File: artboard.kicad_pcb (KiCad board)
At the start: 2 copper layers, 94.7 x 47.4 mm, 25 parts, among them J2 OLED, SW1 SW_PUSH, SW2 SW_PUSH, SW22 SW_SPDT, SW23 SW_SPDT, SW3 SW_PUSH, SW4 SW_PUSH, SW5 SW_PUSH, SW6 SW_PUSH, SW7 SW_PUSH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

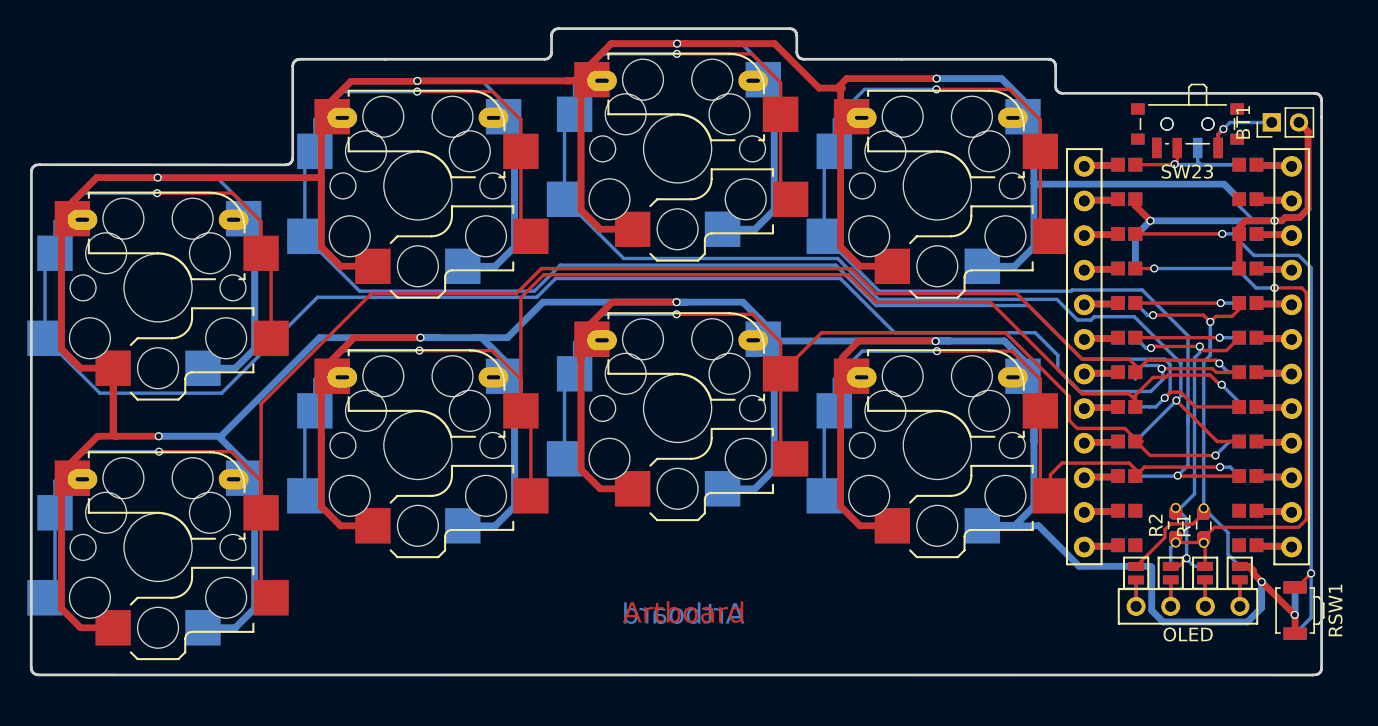
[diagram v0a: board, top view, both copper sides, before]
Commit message: add mounting holes
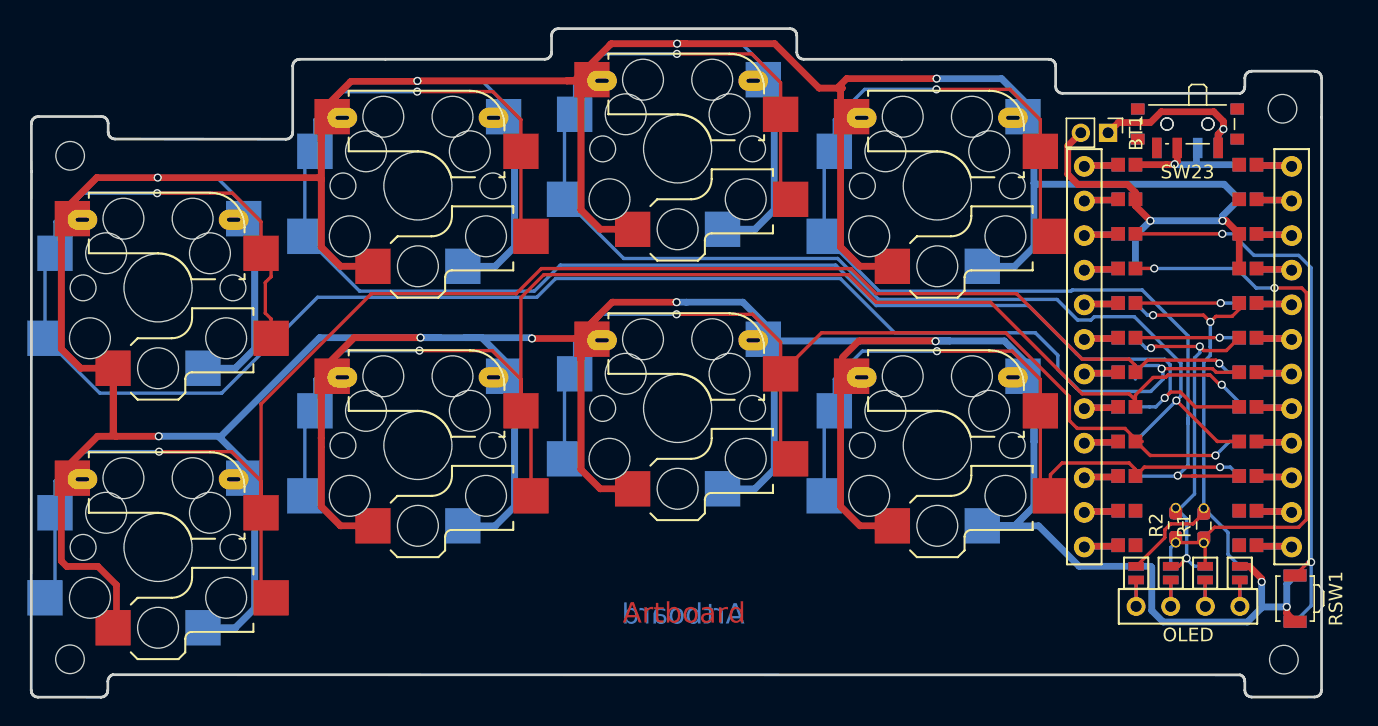
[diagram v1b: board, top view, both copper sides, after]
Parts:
- added Ref**: Val**, MountingHole:MountingHole_2.1mm, F.Cu at (123.8, 76.2)
- added Ref**: Val**, MountingHole:MountingHole_2.1mm, F.Cu at (123.7, 35.8)
- added Ref**: Val**, MountingHole:MountingHole_2.1mm, F.Cu at (34.7, 76.2)
- added Ref**: Val**, MountingHole:MountingHole_2.1mm, F.Cu at (34.7, 39.3)
- moved BT1 12.0 mm to (110.9, 37.6), turned to 270 degrees
- moved RSW1 0.88 mm to (124.7, 71.8)
- moved RSW2 0.88 mm to (124.7, 71.8)
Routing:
- net GND: track 939.4 -> 887.3 mm, vias 12 -> 13
- net Net-(BT1-Pad1): track 6.84 -> 13.1 mm
- net raw: track 15.1 -> 13.0 mm
- net reset: track 43.2 -> 42.3 mm
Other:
- board size 94.7 x 47.4 mm -> 94.7 x 49.1 mm

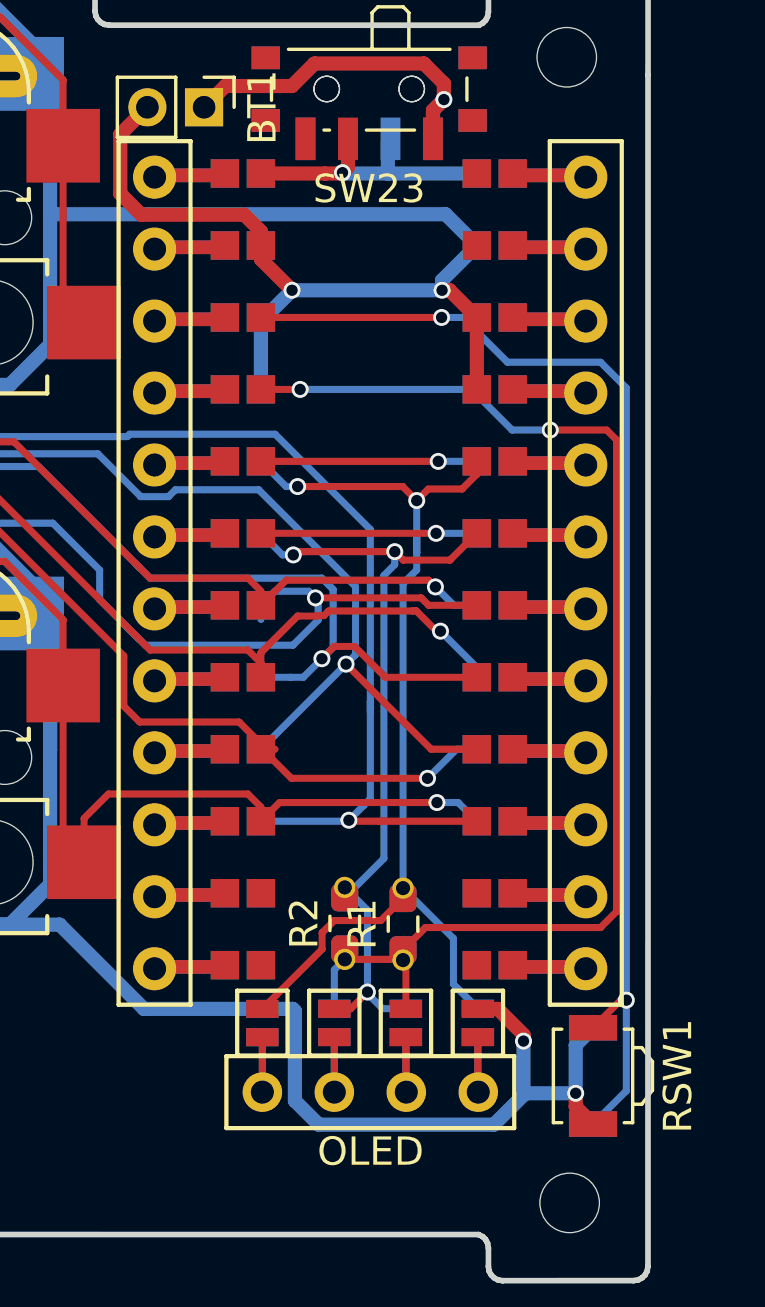
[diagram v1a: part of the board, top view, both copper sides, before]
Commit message: route last dangling pads
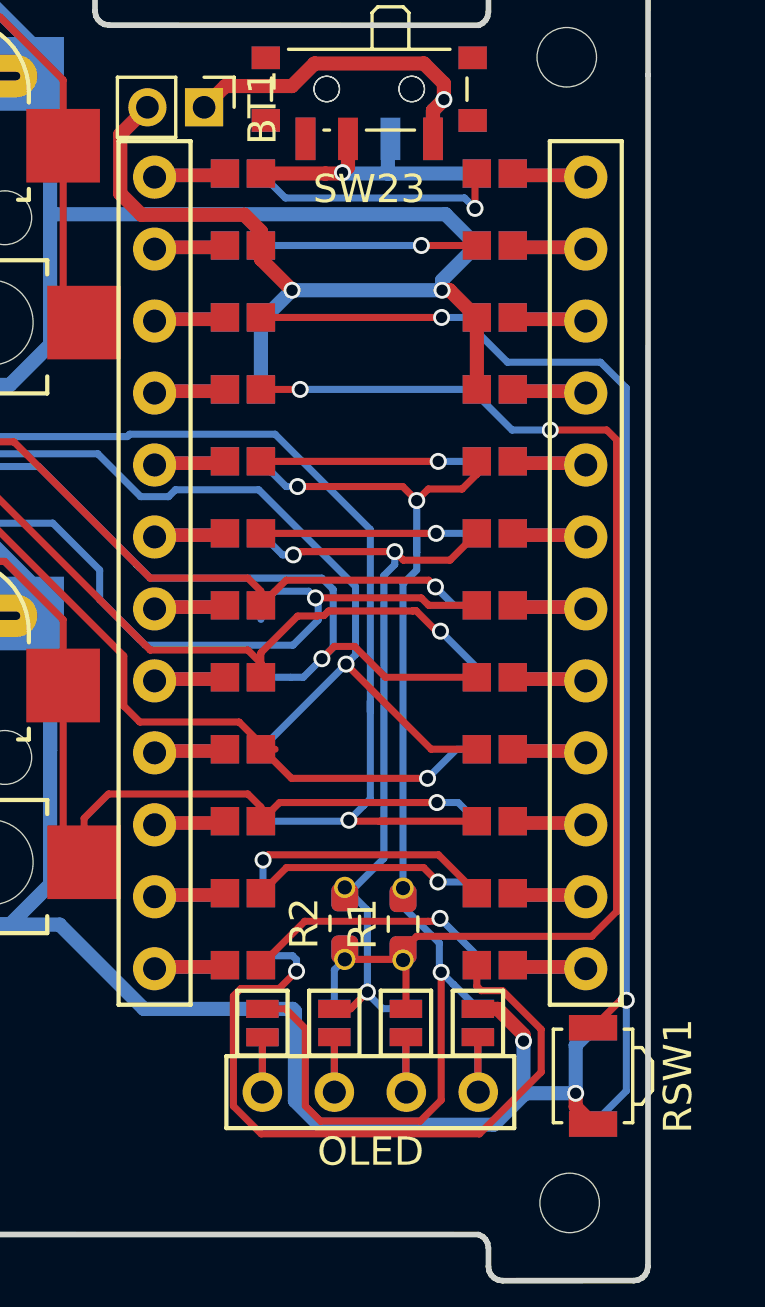
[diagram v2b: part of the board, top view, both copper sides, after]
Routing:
- net Net-(U1-Pad12): track 0.00 -> 25.7 mm, vias 0 -> 1
- net Net-(U1-Pad11): track 0.00 -> 9.38 mm, vias 0 -> 1
- net Net-(U1-Pad1): track 0.00 -> 9.32 mm, vias 0 -> 1
- net Net-(U1-Pad13): track 0.00 -> 9.25 mm, vias 0 -> 1
- net Net-(U1-Pad14): track 0.00 -> 8.37 mm, vias 0 -> 1
- net Net-(U1-Pad2): track 0.00 -> 7.62 mm, vias 0 -> 1
- net SDA: track 35.8 -> 43.3 mm, vias 2 -> 3
